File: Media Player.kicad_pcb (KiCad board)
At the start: 2 copper layers, 124 parts, among them IC2 LM66200DRLR, J1 PH2.0, J2 MEM2075-00-140-01-A, J3 USB_C_Receptacle_USB2.0_14P, J4 UART, J5 SJ-3524-SMT-TR, Q1 DMP3068L-7, Q2 DMP3068L-7, Q3 DMP3068L-7, Q4 DMP3068L-7, SW1 BOOT, SW2 RESET, SW3 SW_Push, SW4 SW_Push, SW5 SW_Push, SW6 SW_Push, SW7 SW_SPST, SW8 SW_SPST, U1 ESP32-S3-WROOM-1, U2 MAX9850xTI, U3 MIC845H, U4 TPS631000DRLR, U5 MCP73831-2-OT

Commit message: Filtered Ratsnest
Moved all related components into their respective groups
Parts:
- moved J5 241.1 mm to (267.0, 73.0)
- moved R10 238.4 mm to (260.1, 84.0)
- moved R11 238.4 mm to (260.1, 87.0)
- moved R12 238.4 mm to (260.1, 89.9)
- moved C23 235.1 mm to (253.0, 92.0)
- moved C26 235.1 mm to (253.0, 95.0)
- moved C27 235.1 mm to (253.0, 98.0)
- moved C28 235.1 mm to (253.0, 101.0)
- moved Q4 234.5 mm to (270.4, 100.3), turned to 180 degrees
- moved R50 226.3 mm to (255.1, 70.0)
- moved R51 226.3 mm to (255.1, 73.0)
- moved R52 226.3 mm to (255.1, 76.0)
- moved C29 224.4 mm to (239.0, 75.0)
- moved R47 214.9 mm to (241.9, 101.9), turned to -90 degrees
- moved R48 212.0 mm to (239.0, 101.9), turned to -90 degrees
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
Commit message: Ratsnest organized
Certain pins on esp32 module changed to benefit layout. Named all decaps to dC. Current layout areas might be not optimal, i.e. complicated to wire
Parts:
- removed TP12: ESP_3V3, TestPoint:TestPoint_Pad_1.5x1.5mm
- added R56: 0Ω, Resistor_SMD:R_0805_2012Metric, F.Cu at (63.1, 99.9)
- added R57: 0Ω, Resistor_SMD:R_0805_2012Metric, F.Cu at (62.9, 96.9)
- added R58: 0Ω, Resistor_SMD:R_0805_2012Metric, F.Cu at (75.1, 86.9)
- added R59: 0Ω, Resistor_SMD:R_0805_2012Metric, F.Cu at (171.5, 139.6)
- added R60: 0Ω, Resistor_SMD:R_0805_2012Metric, F.Cu at (220.6, 56.6)
- C19, C29: footprint Capacitor_SMD:C_0805_2012Metric_Pad1.18x1.45mm_HandSolder -> Capacitor_SMD:C_0603_1608Metric_Pad1.08x0.95mm_HandSolder
- R53, R54, R55: value 0Ω -> NC
- dC1: renamed from C1; footprint Capacitor_SMD:C_0805_2012Metric_Pad1.18x1.45mm_HandSolder -> Capacitor_SMD:C_0603_1608Metric_Pad1.08x0.95mm_HandSolder
- dC10: renamed from C10; footprint Capacitor_SMD:C_0805_2012Metric_Pad1.18x1.45mm_HandSolder -> Capacitor_SMD:C_0603_1608Metric_Pad1.08x0.95mm_HandSolder
- dC11: renamed from C11; footprint Capacitor_SMD:C_0805_2012Metric_Pad1.18x1.45mm_HandSolder -> Capacitor_SMD:C_0603_1608Metric_Pad1.08x0.95mm_HandSolder
- dC13: renamed from C13; footprint Capacitor_SMD:C_0805_2012Metric_Pad1.18x1.45mm_HandSolder -> Capacitor_SMD:C_0603_1608Metric_Pad1.08x0.95mm_HandSolder
- dC2: renamed from C2; footprint Capacitor_SMD:C_0805_2012Metric_Pad1.18x1.45mm_HandSolder -> Capacitor_SMD:C_0603_1608Metric_Pad1.08x0.95mm_HandSolder
- dC20: renamed from C20; footprint Capacitor_SMD:C_0805_2012Metric_Pad1.18x1.45mm_HandSolder -> Capacitor_SMD:C_0603_1608Metric_Pad1.08x0.95mm_HandSolder
- dC21: renamed from C21; footprint Capacitor_SMD:C_0805_2012Metric_Pad1.18x1.45mm_HandSolder -> Capacitor_SMD:C_0603_1608Metric_Pad1.08x0.95mm_HandSolder
- dC22: renamed from C22; footprint Capacitor_SMD:C_0805_2012Metric_Pad1.18x1.45mm_HandSolder -> Capacitor_SMD:C_0603_1608Metric_Pad1.08x0.95mm_HandSolder
- dC23: renamed from C23; footprint Capacitor_SMD:C_0805_2012Metric_Pad1.18x1.45mm_HandSolder -> Capacitor_SMD:C_0603_1608Metric_Pad1.08x0.95mm_HandSolder
- dC26: renamed from C26; footprint Capacitor_SMD:C_0805_2012Metric_Pad1.18x1.45mm_HandSolder -> Capacitor_SMD:C_0603_1608Metric_Pad1.08x0.95mm_HandSolder
- dC27: renamed from C27; footprint Capacitor_SMD:C_0805_2012Metric_Pad1.18x1.45mm_HandSolder -> Capacitor_SMD:C_0603_1608Metric_Pad1.08x0.95mm_HandSolder
- dC28: renamed from C28; footprint Capacitor_SMD:C_0805_2012Metric_Pad1.18x1.45mm_HandSolder -> Capacitor_SMD:C_0603_1608Metric_Pad1.08x0.95mm_HandSolder
- dC3: renamed from C3; footprint Capacitor_SMD:C_0805_2012Metric_Pad1.18x1.45mm_HandSolder -> Capacitor_SMD:C_0603_1608Metric_Pad1.08x0.95mm_HandSolder
- dC30: renamed from C30; footprint Capacitor_SMD:C_0805_2012Metric_Pad1.18x1.45mm_HandSolder -> Capacitor_SMD:C_0603_1608Metric_Pad1.08x0.95mm_HandSolder
- dC31: renamed from C31; footprint Capacitor_SMD:C_0805_2012Metric_Pad1.18x1.45mm_HandSolder -> Capacitor_SMD:C_0603_1608Metric_Pad1.08x0.95mm_HandSolder
- dC4: renamed from C4; footprint Capacitor_SMD:C_0805_2012Metric_Pad1.18x1.45mm_HandSolder -> Capacitor_SMD:C_0603_1608Metric_Pad1.08x0.95mm_HandSolder
- dC5: renamed from C5; footprint Capacitor_SMD:C_0805_2012Metric_Pad1.18x1.45mm_HandSolder -> Capacitor_SMD:C_0603_1608Metric_Pad1.08x0.95mm_HandSolder
- moved C18 127.7 mm to (228.5, 149.0), turned to 90 degrees
- moved SW6 126.8 mm to (220.1, 148.0)
- moved C17 106.9 mm to (227.5, 140.0), turned to 90 degrees
- moved SW5 106.4 mm to (219.5, 139.0)
- moved C12 87.0 mm to (227.5, 131.0), turned to 90 degrees
- moved SW1 86.8 mm to (219.1, 130.0)
- moved dC5 71.8 mm to (96.5, 159.3), turned to -90 degrees
- moved R19 68.8 mm to (82.5, 135.2), turned to -90 degrees
- moved J1 68.6 mm to (174.0, 149.5), turned to 0 degrees
- moved R16 68.4 mm to (92.4, 153.3), turned to 180 degrees
- moved dC30 67.7 mm to (101.5, 154.3)
- moved R15 67.7 mm to (92.6, 156.3)
- moved R54 67.6 mm to (168.5, 139.4)
- moved dC11 67.1 mm to (174.5, 145.5), turned to 0 degrees
- moved Q3 66.9 mm to (167.4, 144.6), turned to 180 degrees
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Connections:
- J1 pad 1: Net-(J1-Pin_1) -> /LCD_VDD
- J2 pad P3: /SD_CMD -> Net-(J2-CMD)
- J2 pad P4: Net-(J2-VDD) -> /SD_VDD
- J2 pad P5: /SD_CLK -> Net-(J2-CLK)
- Q2 pad 1: Net-(J2-VDD) -> /SD_VDD
- Q3 pad 1: Net-(J1-Pin_1) -> /LCD_VDD
- R5 pad 2: ESP_3V3 -> +3V3
- R6 pad 2: ESP_3V3 -> +3V3
- R7 pad 2: ESP_3V3 -> +3V3
- R8 pad 2: ESP_3V3 -> +3V3
- R9 pad 2: ESP_3V3 -> +3V3
- U1 pad 10: /PB0 -> /SD_D3
- U1 pad 11: /PB1 -> /SD_D2
- U1 pad 12: /SD_CMD -> /CHRG_STAT
- U1 pad 17: /SD_CLK -> /PWR_SRC
- U1 pad 18: /LCD_BL -> /LCD_CS_n
- U1 pad 23: /A_GPIO -> /LCD_BL
- U1 pad 24: /A_MCLK -> /PB3
- U1 pad 25: /CHRG_STAT -> /PB2
- U1 pad 31: /A_SLC -> /A_GPIO
- U1 pad 32: /A_SDA -> /A_MCLK
- U1 pad 38: /PB2 -> /A_SDA
- U1 pad 39: /PB3 -> /A_SLC
- U1 pad 4: /SD_D0 -> /PB0
- U1 pad 5: /SD_D1 -> /PB1
- U1 pad 6: /SD_D2 -> /SD_D1
- U1 pad 7: /SD_D3 -> /SD_D0
- U1 pad 8: /LCD_CS_n -> /SD_CLK
- U1 pad 9: /PWR_SRC -> /SD_CMD
- dC10 pad 1: +3V3 -> /SD_VDD
- dC11 pad 1: +3V3 -> /LCD_VDD

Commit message: Component Re-order
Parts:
- removed R3: 0Ω, Resistor_SMD:R_0805_2012Metric
- moved J5 225.2 mm to (38.0, 101.5), turned to 0 degrees
- moved R50 206.6 mm to (39.4, 84.5), turned to 180 degrees
- moved R52 202.6 mm to (43.4, 84.5), turned to 180 degrees
- moved R51 198.7 mm to (47.4, 84.5), turned to 180 degrees
- moved J2 188.4 mm to (232.5, 77.8), turned to 90 degrees
- moved TP1 183.3 mm to (53.5, 64.5), turned to 180 degrees
- moved SW3 180.4 mm to (219.1, 120.0)
- moved C15 180.4 mm to (227.5, 121.0)
- moved dC26 177.8 mm to (51.6, 77.5), turned to 180 degrees
- moved dC20 177.6 mm to (51.6, 79.5), turned to 180 degrees
- moved dC27 177.3 mm to (52.0, 74.5), turned to 90 degrees
- moved TP2 176.4 mm to (57.0, 64.5), turned to 180 degrees
- moved dC28 175.2 mm to (52.6, 84.0), turned to 180 degrees
- moved SW4 174.1 mm to (218.5, 110.5)
- moved dC23 173.3 mm to (54.0, 74.5), turned to 90 degrees
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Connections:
- R4 pad 2: ESP_3V3 -> +3V3
- U1 pad 10: /SD_D3 -> /A_SLC
- U1 pad 11: /SD_D2 -> /PB1
- U1 pad 2: ESP_3V3 -> +3V3
- U1 pad 31: /A_GPIO -> /PB0
- U1 pad 32: /A_MCLK -> /SD_D1
- U1 pad 33: /A_SDIN -> /SD_D0
- U1 pad 34: /A_BCLK -> /SD_CLK
- U1 pad 35: /A_LRCLK -> /SD_CMD
- U1 pad 38: /A_SDA -> /SD_D3
- U1 pad 39: /A_SLC -> /SD_D2
- U1 pad 4: /PB0 -> /A_GPIO
- U1 pad 5: /PB1 -> /A_MCLK
- U1 pad 6: /SD_D1 -> /A_SDIN
- U1 pad 7: /SD_D0 -> /A_BCLK
- U1 pad 8: /SD_CLK -> /A_LRCLK
- U1 pad 9: /SD_CMD -> /A_SDA

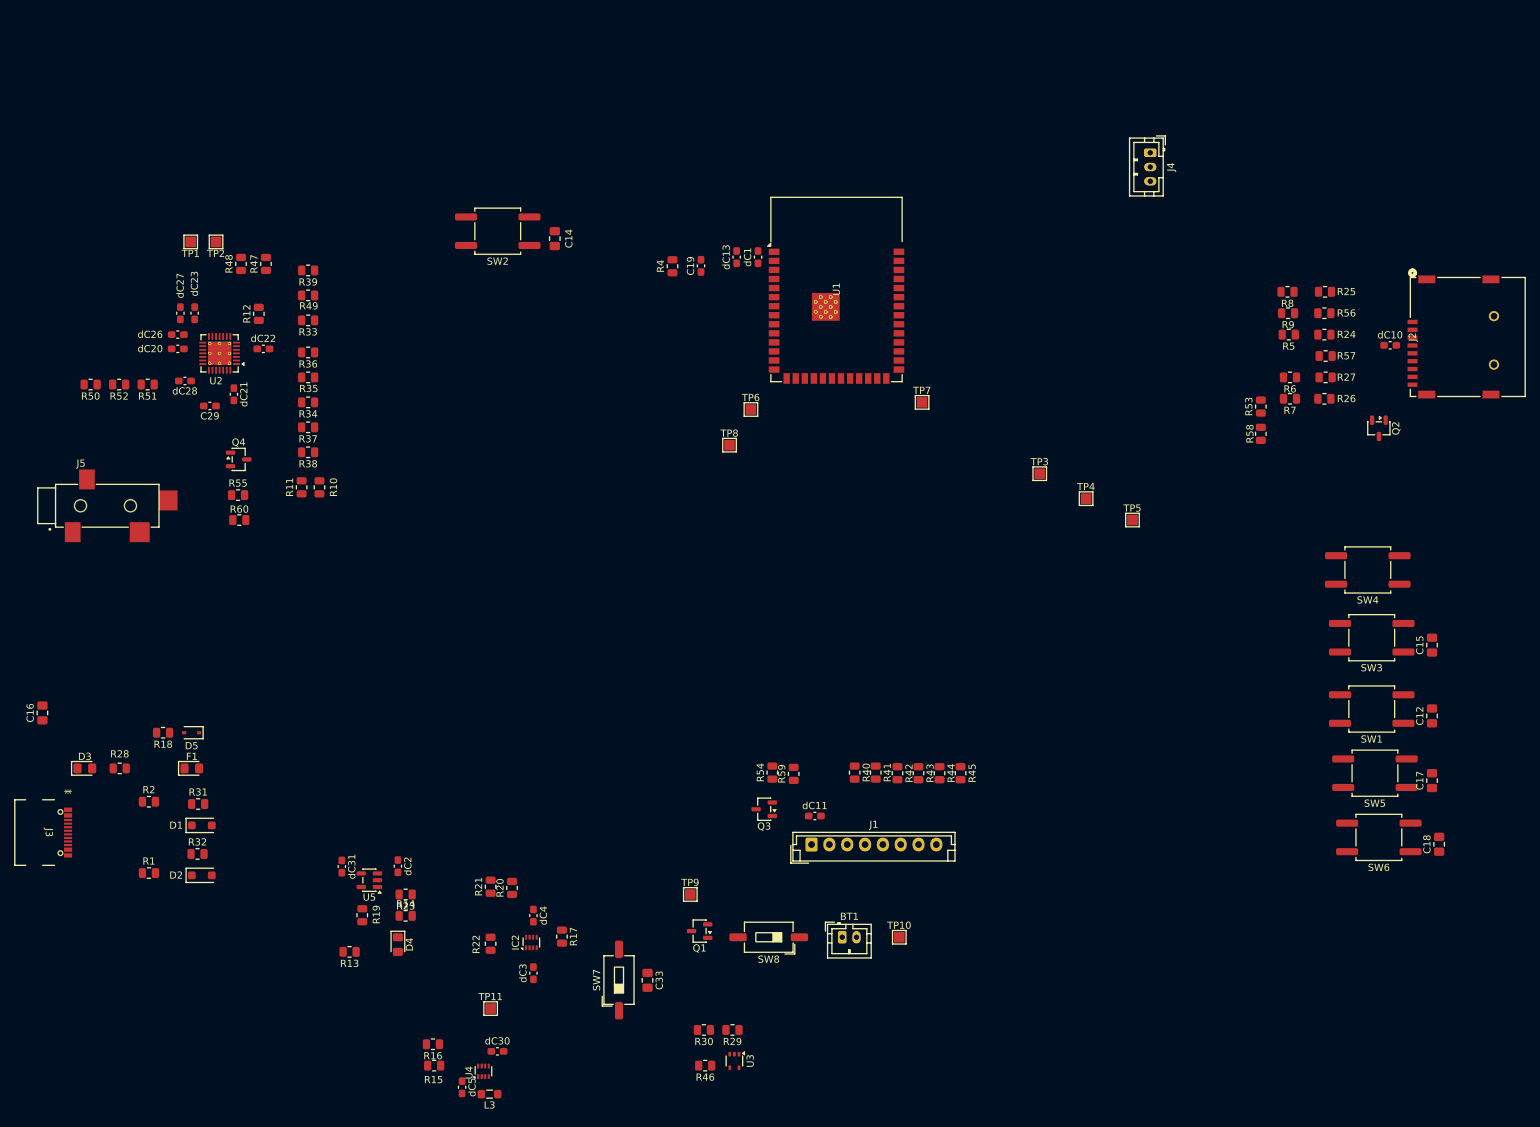
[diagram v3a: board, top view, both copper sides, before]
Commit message: Board stuffing, new audio on board
Added new Audio IC to PCB.
Started moving everything into a estimated board size, AKA restricted area. Things seem REALL TIGHT. There's not enough space, I think I'll have to change resistor footprints
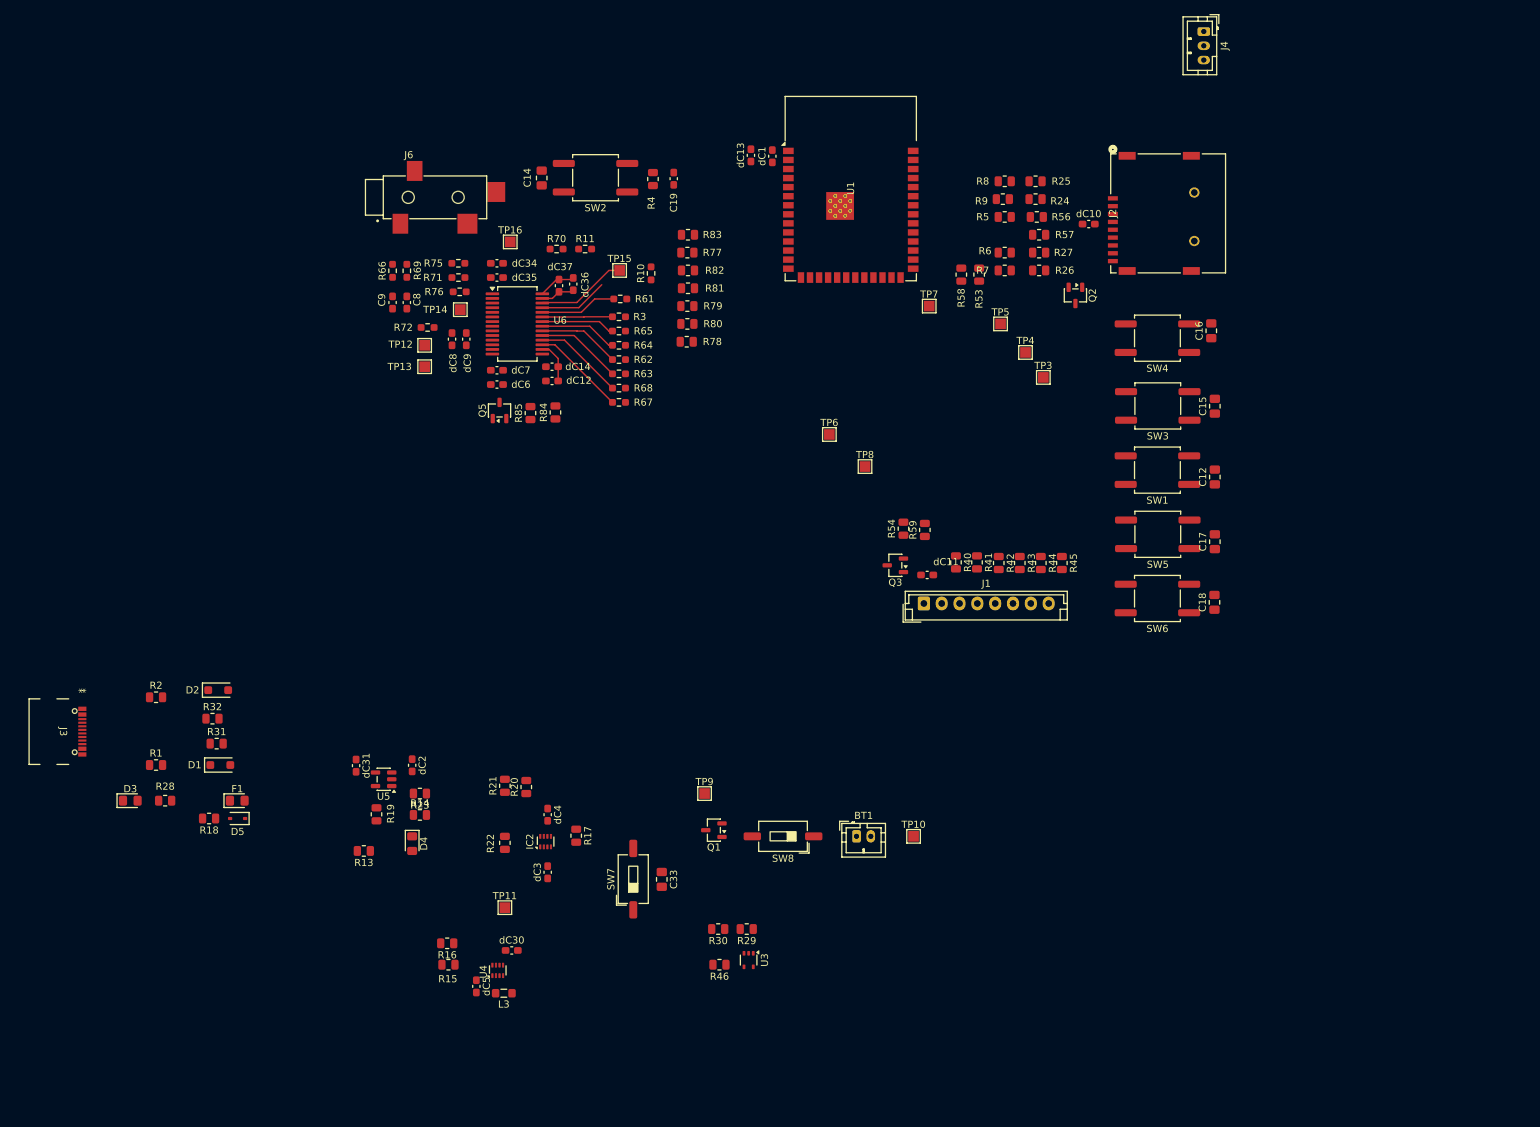
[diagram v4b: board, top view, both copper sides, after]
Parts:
- removed C29: 0.47uF, Capacitor_SMD:C_0603_1608Metric_Pad1.08x0.95mm_HandSolder
- removed J5: SJ-3524-SMT-TR, Footprints:CUI_SJ-3524-SMT
- removed Q4: DMP3068L-7, Package_TO_SOT_SMD:SOT-23-3
- removed R12: 10kΩ, Resistor_SMD:R_0805_2012Metric
- removed R33, R34, R35, R36, R37, R38, R39, R47, R48, R49, R50, R51, R52, R60: 0Ω, Resistor_SMD:R_0805_2012Metric
- removed R55: NC, Resistor_SMD:R_0805_2012Metric
- removed TP1, TP2: Speaker TP, TestPoint:TestPoint_Pad_1.5x1.5mm
- removed U2: MAX9850xTI, Package_DFN_QFN:TQFN-28-1EP_5x5mm_P0.5mm_EP3.25x3.25mm_ThermalVias
- removed dC20, dC21, dC22, dC23, dC26, dC27: 1uF, Capacitor_SMD:C_0603_1608Metric_Pad1.08x0.95mm_HandSolder
- removed dC28: 2.2uF, Capacitor_SMD:C_0603_1608Metric_Pad1.08x0.95mm_HandSolder
- added C8: 220uF, Capacitor_SMD:C_0603_1608Metric_Pad1.08x0.95mm_HandSolder, F.Cu at (83.8, 73.0)
- added C9: 220uF, Capacitor_SMD:C_0603_1608Metric_Pad1.08x0.95mm_HandSolder, F.Cu at (81.8, 73.0)
- added J6: SJ-3524-SMT-TR, Footprints:CUI_SJ-3524-SMT, F.Cu at (84.0, 58.2)
- added Q5: DMP3068L-7, Package_TO_SOT_SMD:SOT-23-3, F.Cu at (96.8, 88.1)
- added R3: 10kΩ, Resistor_SMD:R_0603_1608Metric_Pad0.98x0.95mm_HandSolder, F.Cu at (113.5, 75.0)
- added R61: 10kΩ, Resistor_SMD:R_0603_1608Metric_Pad0.98x0.95mm_HandSolder, F.Cu at (113.7, 72.5)
- added R62: 47kΩ, Resistor_SMD:R_0603_1608Metric_Pad0.98x0.95mm_HandSolder, F.Cu at (113.5, 81.0)
- added R63: 47kΩ, Resistor_SMD:R_0603_1608Metric_Pad0.98x0.95mm_HandSolder, F.Cu at (113.5, 83.0)
- added R64: 10kΩ, Resistor_SMD:R_0603_1608Metric_Pad0.98x0.95mm_HandSolder, F.Cu at (113.5, 79.0)
- added R65: 10kΩ, Resistor_SMD:R_0603_1608Metric_Pad0.98x0.95mm_HandSolder, F.Cu at (113.5, 77.0)
- added R66: 0Ω, Resistor_SMD:R_0603_1608Metric_Pad0.98x0.95mm_HandSolder, F.Cu at (81.8, 68.5)
- added R67: 47kΩ, Resistor_SMD:R_0603_1608Metric_Pad0.98x0.95mm_HandSolder, F.Cu at (113.5, 87.0)
- added R68: 47kΩ, Resistor_SMD:R_0603_1608Metric_Pad0.98x0.95mm_HandSolder, F.Cu at (113.5, 85.0)
- added R69: 0Ω, Resistor_SMD:R_0603_1608Metric_Pad0.98x0.95mm_HandSolder, F.Cu at (83.8, 68.5)
- added R70: 0Ω, Resistor_SMD:R_0603_1608Metric_Pad0.98x0.95mm_HandSolder, F.Cu at (104.8, 65.5)
- added R71: 10kΩ, Resistor_SMD:R_0603_1608Metric_Pad0.98x0.95mm_HandSolder, F.Cu at (91.0, 69.5)
- added R72: 10kΩ, Resistor_SMD:R_0603_1608Metric_Pad0.98x0.95mm_HandSolder, F.Cu at (86.7, 76.5)
- added R75: 100Ω, Resistor_SMD:R_0603_1608Metric_Pad0.98x0.95mm_HandSolder, F.Cu at (91.0, 67.5)
- added R76: 10kΩ, Resistor_SMD:R_0603_1608Metric_Pad0.98x0.95mm_HandSolder, F.Cu at (91.2, 71.5)
- added R77: 0Ω, Resistor_SMD:R_0805_2012Metric, F.Cu at (123.1, 66.0)
- added R78: 0Ω, Resistor_SMD:R_0805_2012Metric, F.Cu at (123.0, 78.5)
- added R79: 0Ω, Resistor_SMD:R_0805_2012Metric, F.Cu at (123.1, 73.5)
- added R80: 0Ω, Resistor_SMD:R_0805_2012Metric, F.Cu at (123.1, 76.0)
- added R81: 0Ω, Resistor_SMD:R_0805_2012Metric, F.Cu at (123.2, 71.0)
- added R82: 0Ω, Resistor_SMD:R_0805_2012Metric, F.Cu at (123.2, 68.5)
- added R83: 0Ω, Resistor_SMD:R_0805_2012Metric, F.Cu at (123.2, 63.5)
- added R84: NC, Resistor_SMD:R_0805_2012Metric, F.Cu at (104.6, 88.4)
- added R85: 0Ω, Resistor_SMD:R_0805_2012Metric, F.Cu at (101.1, 88.5)
- added TP12: LOUT, TestPoint:TestPoint_Pad_1.5x1.5mm, F.Cu at (86.2, 79.0)
- added TP13: ROUT, TestPoint:TestPoint_Pad_1.5x1.5mm, F.Cu at (86.2, 82.0)
- added TP14: ADCDAT, TestPoint:TestPoint_Pad_1.5x1.5mm, F.Cu at (91.2, 74.0)
- added TP15: XTO, TestPoint:TestPoint_Pad_1.5x1.5mm, F.Cu at (113.6, 68.5)
- added TP16: CLKOUT, TestPoint:TestPoint_Pad_1.5x1.5mm, F.Cu at (98.2, 64.5)
- added U6: WM8731SEDS, Package_SO:SSOP-28_5.3x10.2mm_P0.65mm, F.Cu at (99.2, 76.0)
- added dC12: 10uF, Capacitor_SMD:C_0603_1608Metric_Pad1.08x0.95mm_HandSolder, F.Cu at (104.1, 84.0)
- added dC14: 0.1uF, Capacitor_SMD:C_0603_1608Metric_Pad1.08x0.95mm_HandSolder, F.Cu at (104.1, 82.0)
- added dC34: 10uF, Capacitor_SMD:C_0603_1608Metric_Pad1.08x0.95mm_HandSolder, F.Cu at (96.4, 67.5)
- added dC35: 0.1uF, Capacitor_SMD:C_0603_1608Metric_Pad1.08x0.95mm_HandSolder, F.Cu at (96.4, 69.5)
- added dC36: 10uF, Capacitor_SMD:C_0603_1608Metric_Pad1.08x0.95mm_HandSolder, F.Cu at (107.1, 70.4)
- added dC37: 0.1uF, Capacitor_SMD:C_0603_1608Metric_Pad1.08x0.95mm_HandSolder, F.Cu at (105.1, 70.6)
- added dC6: 10uF, Capacitor_SMD:C_0603_1608Metric_Pad1.08x0.95mm_HandSolder, F.Cu at (96.4, 84.5)
- added dC7: 0.1uF, Capacitor_SMD:C_0603_1608Metric_Pad1.08x0.95mm_HandSolder, F.Cu at (96.4, 82.5)
- added dC8: 10uF, Capacitor_SMD:C_0603_1608Metric_Pad1.08x0.95mm_HandSolder, F.Cu at (90.1, 78.1)
- added dC9: 0.1uF, Capacitor_SMD:C_0603_1608Metric_Pad1.08x0.95mm_HandSolder, F.Cu at (92.1, 78.1)
- J3: value USB_C_Receptacle_USB2.0_14P -> USB_C_Receptacle_USB2.0_16P
- R10, R11: footprint Resistor_SMD:R_0805_2012Metric -> Resistor_SMD:R_0603_1608Metric_Pad0.98x0.95mm_HandSolder
- moved C16 172.4 mm to (196.6, 77.0)
- moved R10 55.3 mm to (118.0, 68.9)
- moved R11 51.9 mm to (108.8, 65.5), turned to 0 degrees
- moved R58 47.6 mm to (161.5, 69.1), turned to 90 degrees
- moved Q2 46.5 mm to (177.5, 72.0)
- moved C18 46.3 mm to (197.0, 115.0)
- moved SW6 45.7 mm to (189.0, 114.5)
- moved dC10 45.6 mm to (179.4, 62.0)
- moved J2 45.4 mm to (190.5, 60.5)
- moved C12 45.3 mm to (197.1, 97.5)
- moved C15 45.3 mm to (197.1, 87.5)
- moved C17 45.3 mm to (197.1, 106.5)
- moved SW5 45.3 mm to (189.1, 105.5)
- moved SW1 45.0 mm to (189.0, 96.5)
- moved SW3 44.2 mm to (189.1, 87.5)
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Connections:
- BT1 pad 2: AGND -> GND
- C12 pad 2: AGND -> GND
- C14 pad 2: AGND -> GND
- C15 pad 2: AGND -> GND
- C16 pad 2: AGND -> GND
- C17 pad 2: AGND -> GND
- C18 pad 2: AGND -> GND
- C19 pad 2: AGND -> GND
- C33 pad 2: AGND -> GND
- D1 pad 2: AGND -> GND
- D2 pad 2: AGND -> GND
- D3 pad 1: AGND -> GND
- IC2 pad 1: AGND -> GND
- IC2 pad 5: AGND -> GND
- J1 pad 2: AGND -> GND
- J2 pad P6: AGND -> GND
- J3 pad A1: AGND -> GND
- J3 pad B1: AGND -> GND
- J4 pad 3: AGND -> GND
- Q1 pad 2: AGND -> GND
- R1 pad 2: AGND -> GND
- R10 pad 1: /Audio/AVDD -> /AudioAlt/A2_MCLK
- R10 pad 2: /Audio/SDA -> GND
- R11 pad 1: /Audio/AVDD -> /AudioAlt/A2_TSW
- R11 pad 2: /Audio/SLC -> GND
- R16 pad 2: AGND -> GND
- R18 pad 2: AGND -> GND
- R19 pad 2: AGND -> GND
- R2 pad 2: AGND -> GND
- R20 pad 1: AGND -> GND
- R23 pad 2: AGND -> GND
- R29 pad 1: AGND -> GND
- R58 pad 2: AGND -> GND
- R59 pad 2: AGND -> GND
- SW1 pad 1: AGND -> GND
- SW2 pad 1: AGND -> GND
- SW3 pad 1: AGND -> GND
- SW4 pad 1: AGND -> GND
- SW5 pad 1: AGND -> GND
- SW6 pad 1: AGND -> GND
- SW7 pad 1: AGND -> GND
- TP10 pad 1: AGND -> GND
- U1 pad 1: AGND -> GND
- U1 pad 10: /A_SLC -> /A_LRCLK
- U1 pad 40: AGND -> GND
- U1 pad 41: AGND -> GND
- U1 pad 6: /A_SDIN -> /A_SLC
- U1 pad 7: /A_BCLK -> /A_SDA
- U1 pad 8: /A_LRCLK -> /A_BCLK
- U1 pad 9: /A_SDA -> /A_SDIN
- U3 pad 2: AGND -> GND
- U4 pad 7: AGND -> GND
- U5 pad 2: AGND -> GND
- dC1 pad 2: AGND -> GND
- dC10 pad 2: AGND -> GND
- dC11 pad 2: AGND -> GND
- dC13 pad 2: AGND -> GND
- dC2 pad 1: AGND -> GND
- dC3 pad 1: AGND -> GND
- dC30 pad 2: AGND -> GND
- dC31 pad 1: AGND -> GND
- dC4 pad 1: AGND -> GND
- dC5 pad 2: AGND -> GND
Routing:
- net Net-(U6-MICBIAS): track 0.00 -> 13.4 mm
- net Net-(U6-XTO): track 0.00 -> 12.7 mm
- net Net-(U6-MICIN): track 0.00 -> 12.6 mm
- net Net-(U6-RLINEIN): track 0.00 -> 12.1 mm
- net Net-(U6-LLINEIN): track 0.00 -> 11.5 mm
- net /AudioAlt/A2_SCLK: track 0.00 -> 11.0 mm
- net Net-(U6-MODE): track 0.00 -> 10.9 mm
- net Net-(U6-~{CSB}): track 0.00 -> 10.4 mm
- net /AudioAlt/A2_SDIN: track 0.00 -> 9.85 mm
- net /AudioAlt/A2_MCLK: track 0.00 -> 9.67 mm
- net /AudioAlt/VMID: track 0.00 -> 5.90 mm
- net GND: track 0.00 -> 5.26 mm
- net /AudioAlt/AVDD: track 0.00 -> 4.81 mm
